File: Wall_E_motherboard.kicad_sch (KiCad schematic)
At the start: 50 parts, among them J1 Conn_01x02, J2 Conn_01x06_Socket, J3 Conn_01x06_Socket, J4 Conn_01x06_Socket, J5 Conn_01x06_Socket, J6 Conn_01x04_Socket, J7 Conn_02x09_Counter_Clockwise, J8 Conn_01x06_Socket, SW3 SW_SPST, U2 STM32F411RCTx, U3 DRV8838, U4 DRV8838, U5 DRV8838, U6 BNO055, U7 DRV8838, Y1 25MHz, Y2 32.768kHz, Y3 32.168k

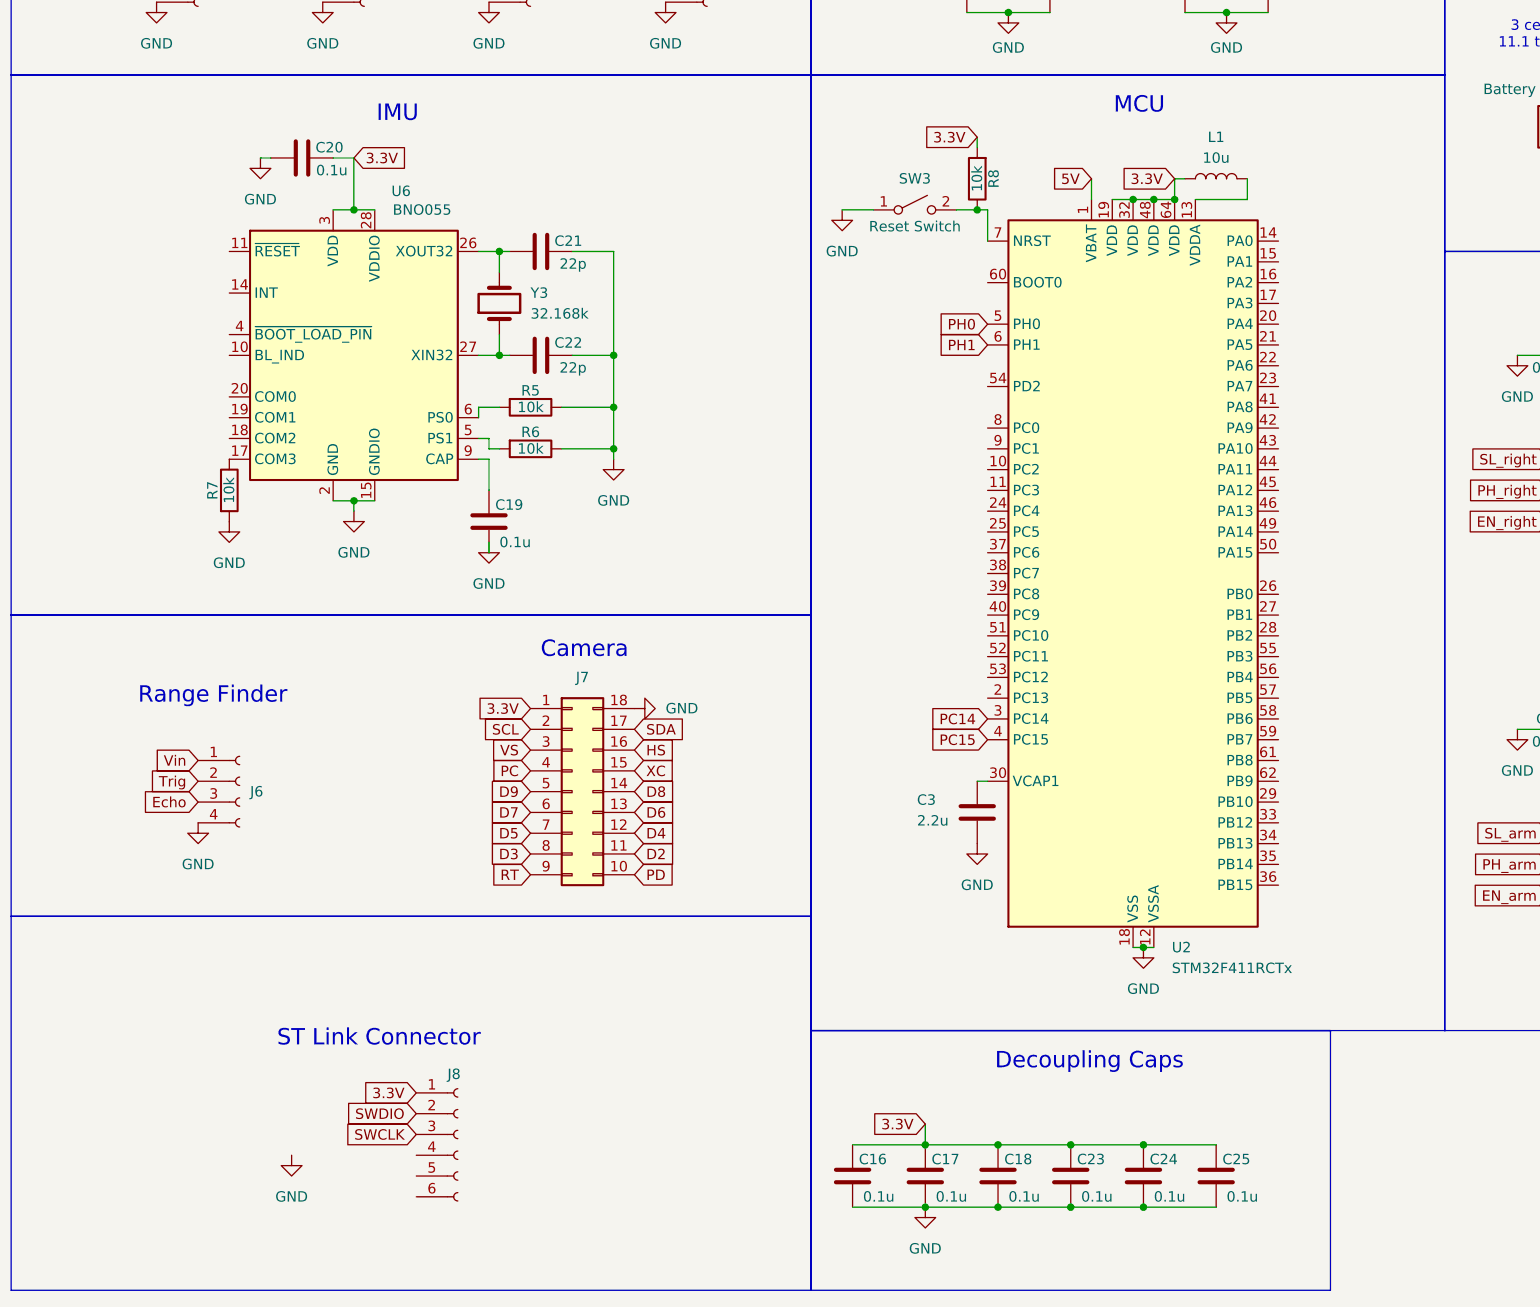
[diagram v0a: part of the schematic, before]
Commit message: Added some footprints and made some connections
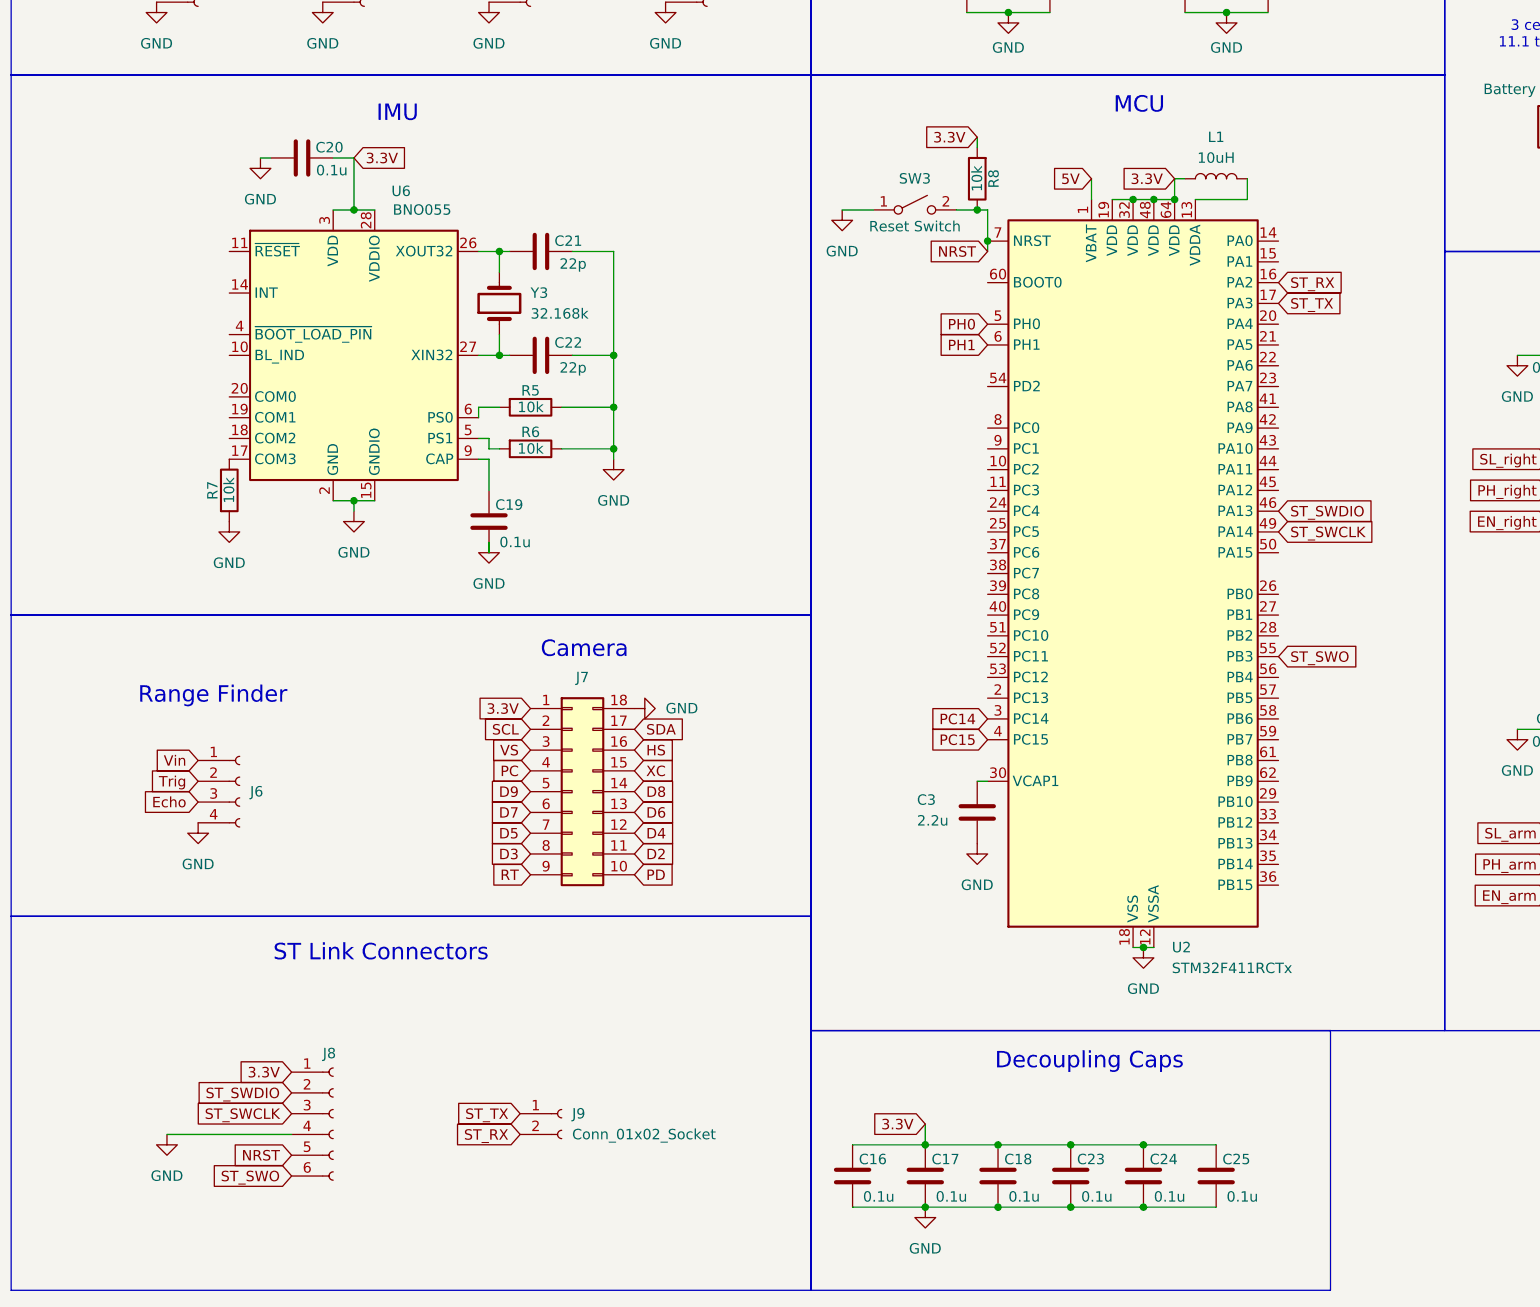
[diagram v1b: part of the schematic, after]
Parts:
- added J9: Conn_01x02_Socket, symbol Connector:Conn_01x02_Socket
- C10, C11, C12, C13, C14, C15, C16, C17, C18, C19, C20, C21, C22, C23, C24, C25, C3, C4, C5, C6, C7, C8, C9: footprint (none) -> Capacitor_SMD:C_0603_1608Metric
- D2: footprint (none) -> LED_SMD:LED_0603_1608Metric
- L1: value 10u -> 10uH
- R3, R4, R5, R6, R7, R8: footprint (none) -> Resistor_SMD:R_0603_1608Metric
- SW3: footprint (none) -> Button_Switch_THT:SW_PUSH_6mm
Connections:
- net SWCLK is gone; now on net ST_SWCLK: J8.3 (Pin_3)
- net SWDIO is gone; now on net ST_SWDIO: J8.2 (Pin_2)
- net GND: now also J8.4 (Pin_4)
- net NRST: now reaches R8.1, SW3.2 (B), U2.7 (NRST)
- net NRST: now also J8.5 (Pin_5)
- net ST_RX: now reaches U2.16 (PA2)
- net ST_RX: now also J9.2 (Pin_2)
- net ST_TX: now reaches U2.17 (PA3)
- net ST_TX: now also J9.1 (Pin_1)
- net ST_SWDIO: now reaches U2.46 (PA13)
- net ST_SWCLK: now reaches U2.49 (PA14)
- net ST_SWO: now reaches U2.55 (PB3)
- net ST_SWO: now also J8.6 (Pin_6)
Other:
- note added: "ST Link Connectors"
- note removed: "ST Link Connector"
- moved on the sheet: J8

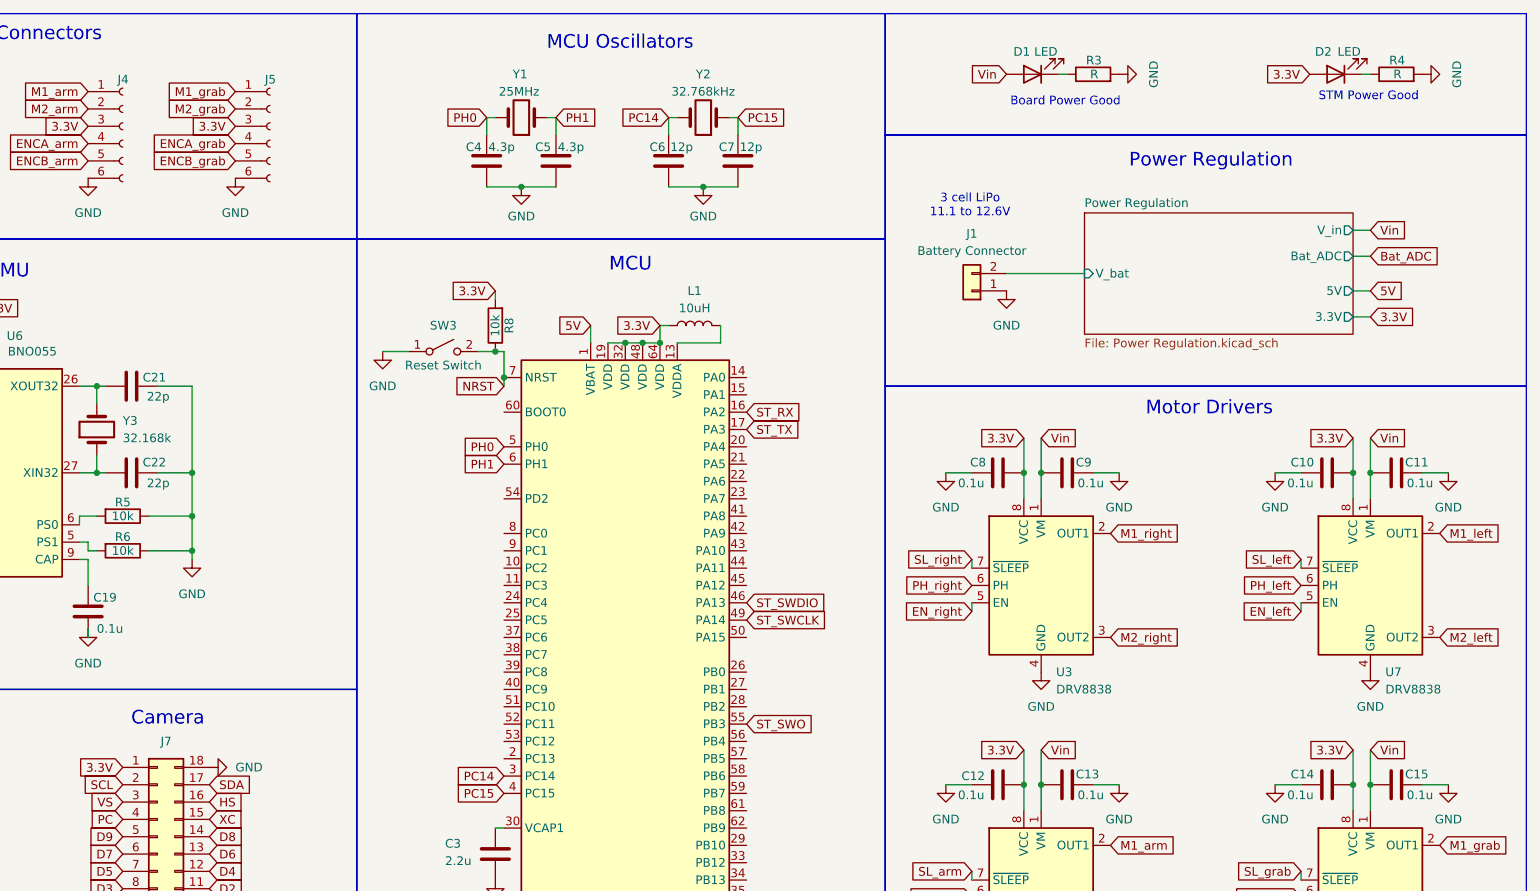
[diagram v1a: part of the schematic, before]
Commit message: initial routing of power and MCU sections
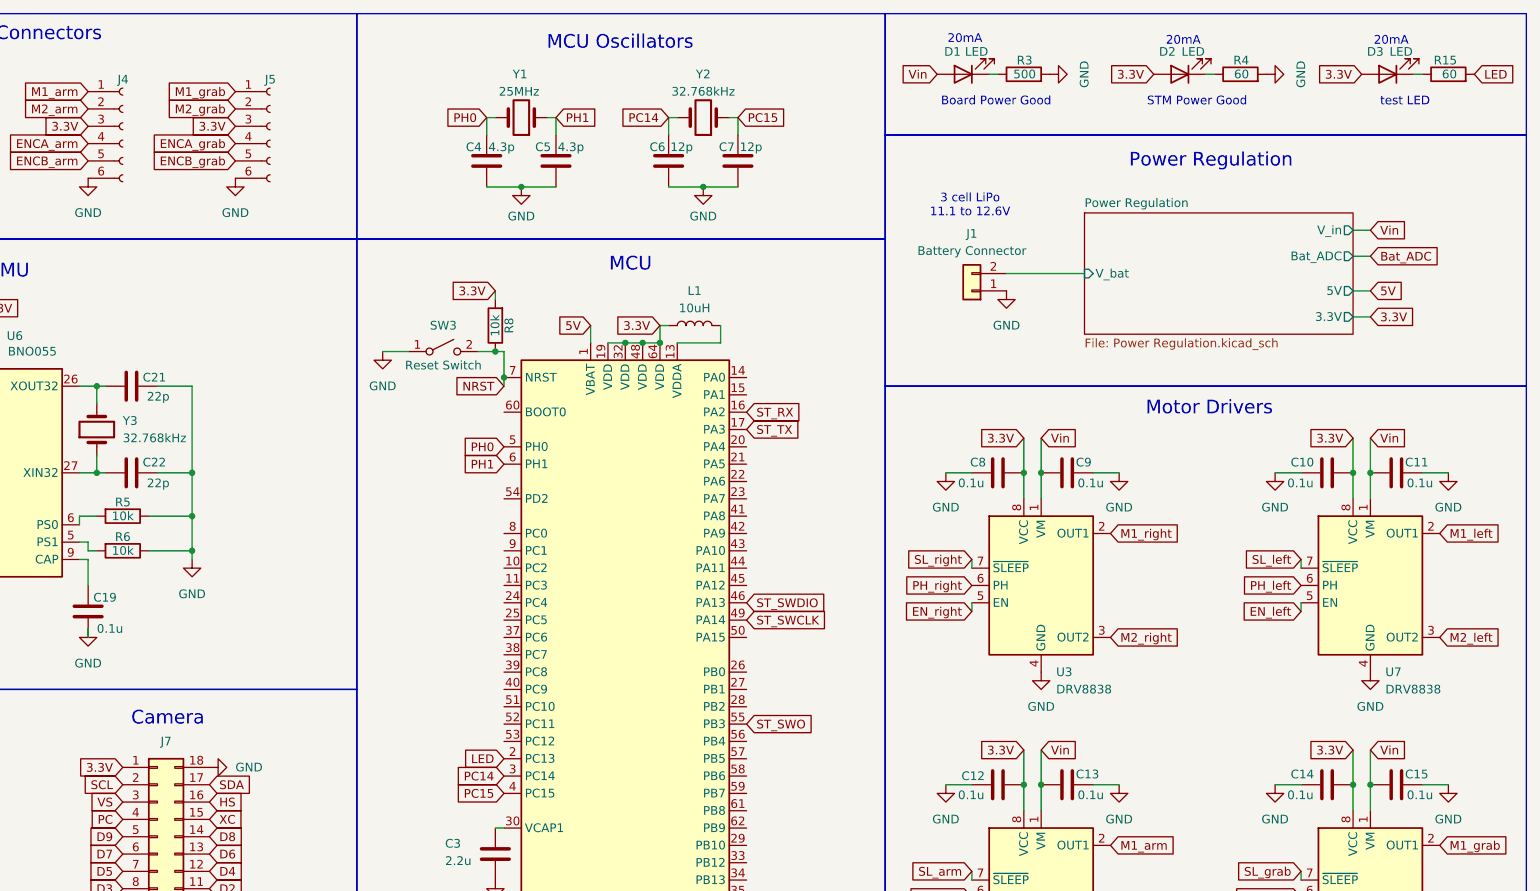
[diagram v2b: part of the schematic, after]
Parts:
- added D3: LED, LED_SMD:LED_0603_1608Metric, symbol Device:LED
- added R15: 60, Resistor_SMD:R_0603_1608Metric, symbol Device:R
- J1: footprint (none) -> Connector_AMASS:AMASS_XT30PW-M_1x02_P2.50mm_Horizontal
- J8: footprint (none) -> Connector_PinHeader_2.54mm:PinHeader_1x06_P2.54mm_Horizontal
- J9: footprint (none) -> Connector_PinHeader_2.54mm:PinHeader_1x02_P2.54mm_Horizontal
- L1: footprint (none) -> Inductor_SMD:L_1008_2520Metric
- R3: value R -> 500
- R4: value R -> 60
- Y1, Y2: footprint (none) -> Crystal:Crystal_SMD_HC49-SD
- Y3: value 32.168k -> 32.768kHz; footprint (none) -> Crystal:Crystal_SMD_HC49-SD
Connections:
- net 3.3V: now also D3.2 (A)
- net LED: now reaches U2.2 (PC13)
- net LED: now also R15.2
- new net: D3.1 (K), R15.1
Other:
- note added: "20mA"
- note added: "test LED"
- moved on the sheet: D1, D2, R3, R4

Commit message: Routing Updates
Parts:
- removed C11, C9: 0.1u, Capacitor_SMD:C_0603_1608Metric, symbol Device:C
- added ArmL1, ArmR1, HandL1, HandR1: Conn_01x03_Socket, Connector_PinHeader_2.54mm:PinHeader_1x03_P2.54mm_Vertical, symbol Connector:Conn_01x03_Socket
- added C11, C9: 22u, Capacitor_THT:CP_Radial_D5.0mm_P2.00mm, symbol Device:C_Polarized
- added Camera1: Conn_01x08_Socket, Connector_PinHeader_2.54mm:PinHeader_1x08_P2.54mm_Vertical, symbol Connector:Conn_01x08_Socket
- added H1, H2, H3, H4: MountingHole, MountingHole:MountingHole_3.2mm_M3, symbol Mechanical:MountingHole
- added J15: USB_C_Receptacle_USB2.0_14P, symbol Connector:USB_C_Receptacle_USB2.0_14P
- added R16, R17: 10, Resistor_SMD:R_0603_1608Metric, symbol Device:R
- added R18, R19: 10k, Resistor_SMD:R_0603_1608Metric, symbol Device:R
- LeftMotor1: renamed from J3; footprint (none) -> Connector_PinHeader_2.54mm:PinHeader_1x06_P2.54mm_Vertical
- Range1: renamed from J6; footprint (none) -> Connector_PinHeader_2.54mm:PinHeader_1x04_P2.54mm_Vertical
- RightMotor1: renamed from J2; footprint (none) -> Connector_PinHeader_2.54mm:PinHeader_1x06_P2.54mm_Vertical
- SW3: footprint Button_Switch_THT:SW_PUSH_6mm -> Button_Switch_SMD:SW_SPST_PTS645
- Y1: footprint Crystal:Crystal_SMD_HC49-SD -> Crystal:Crystal_SMD_3225-4Pin_3.2x2.5mm
- Y2, Y3: footprint Crystal:Crystal_SMD_HC49-SD -> Crystal:Crystal_SMD_3215-2Pin_3.2x1.5mm
- renumbered J8 to STLink1, J9 to UART1
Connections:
- net PH_left is gone; now on net DIR_left: U7.6 (PH)
- net PH_right is gone; now on net DIR_right: U3.6 (PH)
- net 3.3V: now also U2.1 (VBAT), U6.4 (~{BOOT_LOAD_PIN}), R18.1, R19.1
- net 5V: now also Range1.1 (Pin_1), Camera1.3 (Pin_3); no longer U2.1 (VBAT)
- net Bat_ADC: now also U2.15 (PA1)
- net ENCA_left: now also U2.14 (PA0)
- net ENCA_right: now also U2.59 (PB7)
- net ENCB_left: now also U2.29 (PB10)
- net ENCB_right: now also U2.61 (PB8)
- net Echo: now also U2.22 (PA6)
- net GND: now also U6.10 (BL_IND), U6.18 (COM2), ArmL1.1 (Pin_1), ArmR1.1 (Pin_1), C11.2, C9.2, Camera1.4 (Pin_4), HandL1.1 (Pin_1), HandR1.1 (Pin_1), J15.A1 (GND), J15.A12 (GND), J15.B1 (GND), J15.B12 (GND), J15.S1 (SHIELD); no longer C21.2, C22.2
- net Trig: now also U2.23 (PA7)
- net Vin: now also ArmL1.2 (Pin_2), ArmR1.2 (Pin_2), C11.1, C9.1, HandL1.2 (Pin_2), HandR1.2 (Pin_2); no longer Range1.1 (Pin_1)
- net CAM_SCLK: now reaches U2.21 (PA5)
- net CAM_SCLK: now also Camera1.5 (Pin_5)
- net DIR_left: now reaches U2.26 (PB0)
- net DIR_right: now reaches U2.27 (PB1)
- net R_Arm_PWM: now reaches U2.41 (PA8)
- net R_Arm_PWM: now also ArmR1.3 (Pin_3)
- net L_Arm_PWM: now reaches U2.42 (PA9)
- net L_Arm_PWM: now also ArmL1.3 (Pin_3)
- net R_Hand_PWM: now reaches U2.43 (PA10)
- net R_Hand_PWM: now also HandR1.3 (Pin_3)
- net L_Hand_PWM: now reaches U2.44 (PA11)
- net L_Hand_PWM: now also HandL1.3 (Pin_3)
- net CAM_CS: now reaches U2.53 (PC12)
- net CAM_CS: now also Camera1.8 (Pin_8)
- net CAM_MISO: now reaches U2.56 (PB4)
- net CAM_MISO: now also Camera1.6 (Pin_6)
- net CAM_MOSI: now reaches U2.57 (PB5)
- net CAM_MOSI: now also Camera1.7 (Pin_7)
- net I2C_SCL: now reaches U2.58 (PB6)
- net I2C_SCL: now also U6.19 (COM1), Camera1.1 (Pin_1), R19.2
- net I2C_SDA: now reaches U2.62 (PB9)
- net I2C_SDA: now also U6.20 (COM0), Camera1.2 (Pin_2), R18.2
- net IMU_PS0: now reaches R5.2, U6.6 (PS0)
- net IMU_PS1: now reaches R6.2, U6.5 (PS1)
- net IMU_NRST: now reaches U6.11 (~{RESET})
- net IMU_INT: now reaches U6.14 (INT)
- new net: J15.A6 (D+), J15.B6 (D+), R17.1
- new net: C21.2, C22.2
- new net: J15.A7 (D-), J15.B7 (D-), R16.1
- new net: J15.A4 (VBUS), J15.A9 (VBUS), J15.B4 (VBUS), J15.B9 (VBUS)
- new net USBD+: R17.2
- new net USBD-: R16.2
- no-connect marks 0 -> 21
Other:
- note added: "I2C Pullups"
- note added: "Servo Motor Connectors"
- note added: "This pull down sets the I2C addr to 0x28"
- note added: "USB-C"
- moved on the sheet: C12, C13, C14, C15, C19, C20, C21, C22, J4, J5, J7, LeftMotor1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

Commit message: continued routing
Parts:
- removed C12, C13, C14, C15: 0.1u, Capacitor_SMD:C_0603_1608Metric, symbol Device:C
- removed J15: USB_C_Receptacle_USB2.0_14P, symbol Connector:USB_C_Receptacle_USB2.0_14P
- removed J4, J5: Conn_01x06_Socket, symbol Connector:Conn_01x06_Socket
- removed J7: Conn_02x09_Counter_Clockwise, symbol Connector_Generic:Conn_02x09_Counter_Clockwise
- removed R16, R17: 10, Resistor_SMD:R_0603_1608Metric, symbol Device:R
- removed U4, U5: DRV8838, Package_SON:WSON-8-1EP_2x2mm_P0.5mm_EP0.9x1.6mm, symbol Driver_Motor:DRV8838
- added TP1, TP2: TestPoint_Small, TestPoint:TestPoint_Pad_D1.0mm, symbol Connector:TestPoint_Small
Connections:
- net DIR_left: now also TP1.1
- net DIR_right: now also TP2.1
- net EN_right: now also U2.50 (PA15)
- net L_Arm_PWM: now also U2.41 (PA8); no longer U2.42 (PA9)
- net L_Hand_PWM: now also U2.42 (PA9); no longer U2.44 (PA11)
- net R_Arm_PWM: now also U2.44 (PA11); no longer U2.41 (PA8)
- net SL_left: now also U2.25 (PC5)
- net SL_right: now also U2.28 (PB2)
- no-connect marks 21 -> 18
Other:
- note removed: "USB-C"
